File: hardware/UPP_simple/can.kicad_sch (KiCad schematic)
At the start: 16 parts, among them J1 Conn_01x02, U10 ADM3057ExRW

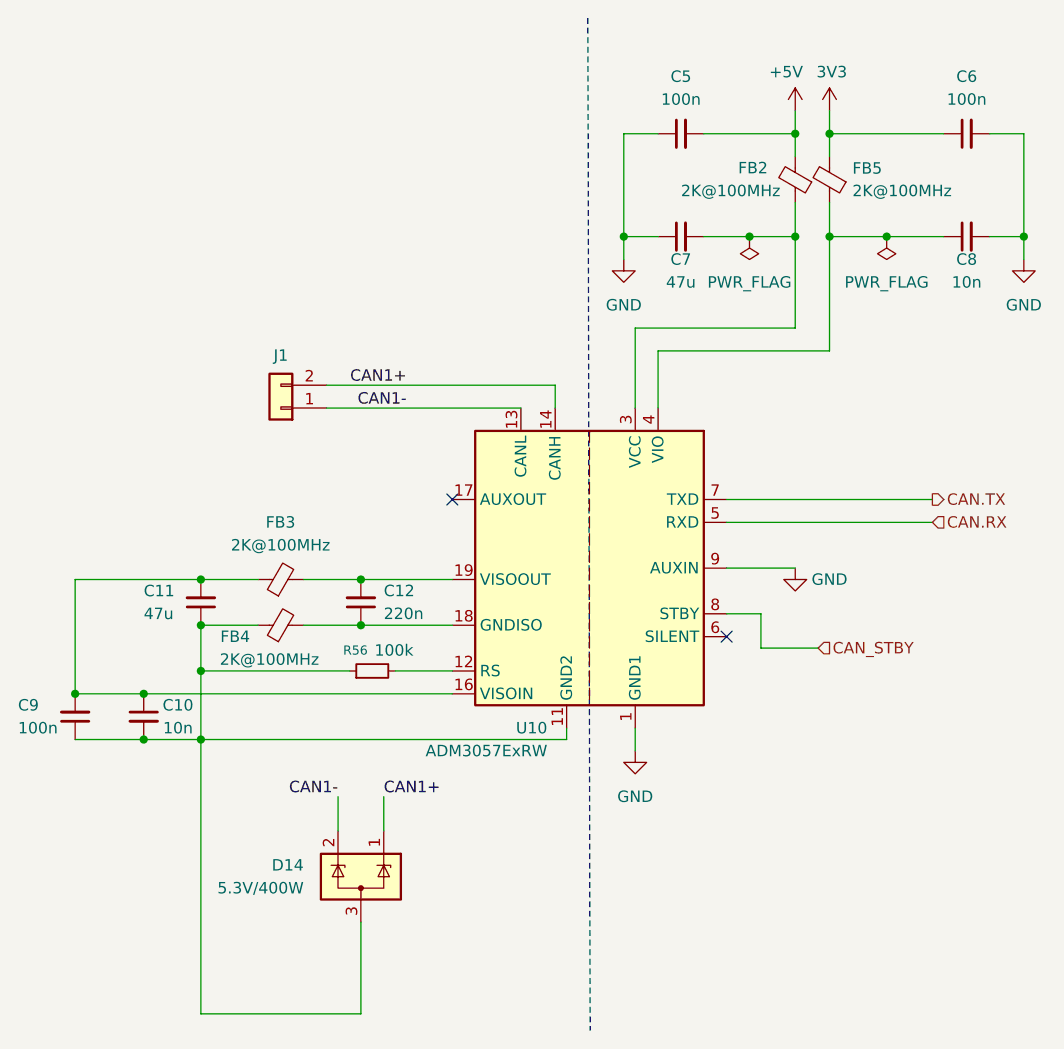
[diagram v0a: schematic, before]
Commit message: Changed Opamps cleared schematic
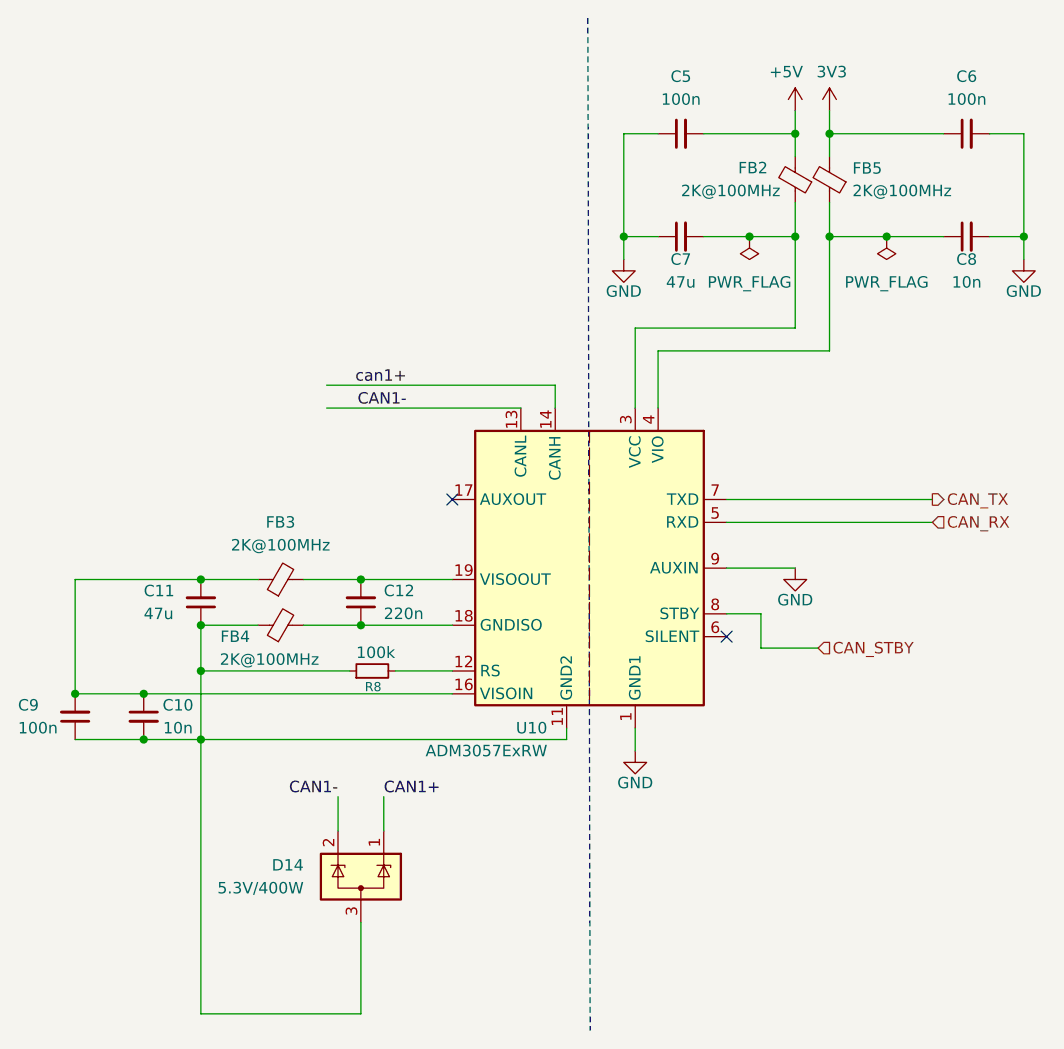
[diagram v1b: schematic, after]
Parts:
- removed J1: Conn_01x02, symbol Connector_Generic:Conn_01x02
- renumbered R56 to R8
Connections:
- net CAN1+: no longer U10.14 (CANH)
- net CAN.RX renamed CAN_RX
- net CAN.TX renamed CAN_TX
- new net can1+: U10.14 (CANH)
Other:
- title: Universal use measuring PCB -> Universal Measurement Board
